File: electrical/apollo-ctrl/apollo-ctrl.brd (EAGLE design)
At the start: 100 x 80 mm, 24 parts, among them J1 BARREL-JACK, Q1 N-chan, U1 NANO

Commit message: DIY version of PCB sort of done, require review
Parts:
- added BAT1: (no value), apollo-ctrl:BATTERY-AA-KIT
- added C1: 47u or more, apollo-ctrl:CPOL-RADIAL-1000UF-25V
- added C2: 100n, apollo-ctrl:CAP-PTH-SMALL
- added COIL2: (no value), apollo-ctrl:SCREWTERMINAL-3.5MM-2
- added D10, D11, D12: 3V6, apollo-ctrl:DIODE-1N4148
- added D4, D5: (no value), apollo-ctrl:DIODE-1N4001
- added D6, D7, D8, D9: (no value), apollo-ctrl:DIODE-1N4148
- added F3: PTC, apollo-ctrl:PTC
- added JP7, JP8: STAND-OFF, apollo-ctrl:STAND-OFF
- added LOGO1: APOLLO-LOGO, apollo-ctrl:APOLLO-LOGO
- added OK2: PC817, apollo-ctrl:DIL04
- added Q2: N-chan, apollo-ctrl:TO220V
- added R10, R11, R12, R13, R14, R15, R7, R8: 620R, apollo-ctrl:AXIAL-0.4
- added R6, R9: 10K, apollo-ctrl:AXIAL-0.4
- added S1: (no value), apollo-ctrl:TACTILE-PTH
- added TVS3, TVS4, TVS5, TVS6, TVS7: TVS 16V, apollo-ctrl:DIODE-1N4148
- added U2: HONEYWELL-MPR, apollo-ctrl:HONEYWELL-MPR-GAGE-DIY
- added X2: SENSOR-O2, apollo-ctrl:JST-PH-4-VERT
- added X3: (no value), apollo-ctrl:1X05
- D1: value (none) -> 3V6
- D2: device apollo-ctrl:DIODE-1N4148 -> apollo-ctrl:DIODE-1N4001
- F1: value PTC -> FUSE 3A; device apollo-ctrl:PTC -> apollo-ctrl:FUSE-KEYSTONE-3568
- F2: value FUSE 3A -> PTC; device apollo-ctrl:FUSE-KEYSTONE-3568 -> apollo-ctrl:PTC
- LED1: value (none) -> GRN
- LED2: value (none) -> RED
- R1: value 1K -> 470R 500mW; device apollo-ctrl:AXIAL-0.4 -> apollo-ctrl:AXIAL-0.5
- R5: value 1K -> 4K7
- SG1: value BUZZER-POL-AI-3035 -> BUZZER
- TVS1: device apollo-ctrl:SMA-DIODE -> apollo-ctrl:DIODE-1N4148
- TVS2: value TVS -> TVS 16V; device apollo-ctrl:SMA-DIODE -> apollo-ctrl:DIODE-1N4148
- moved D2 125.7 mm to (50.0, 52.5)
- moved R5 108.9 mm to (19.5, 49.5)
- moved R4 106.4 mm to (19.5, 52.0)
- moved TVS2 94.0 mm to (69.5, 14.0), turned to 180 degrees
- moved JP3 94.0 mm to (97.0, 77.0)
- moved JP4 94.0 mm to (3.00, 77.0)
- moved TVS1 90.3 mm to (69.5, 11.5)
- moved OK1 90.0 mm to (69.5, 26.5)
- moved D1 84.9 mm to (50.0, 50.0), turned to 180 degrees
- moved LED1 77.2 mm to (58.0, 77.0), turned to 180 degrees
- moved LED2 77.2 mm to (65.0, 77.0), turned to 180 degrees
- moved COIL1 71.6 mm to (67.5, 4.00)
- moved R1 65.2 mm to (50.0, 45.0), turned to 180 degrees
- moved Q1 63.1 mm to (61.0, 15.0), turned to 270 degrees
- moved F1 63.1 mm to (22.0, 11.0)
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- renumbered J1 to X1
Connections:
- removed net N$1: COIL1.2, D1.C, TVS2.C
- new net 3.3V: C2.1, R4.P$2, R5.P$2, U1.3.3V, U2.12
- new net 5V: D4.C, U1.5V, X2.4, X3.5
- new net AUX: U1.D12, X3.2
- new net BUTTON: S1.1, S1.2, TVS5.C, U1.D11
- new net BUZZ: SG1.P, U1.D8
- new net COIL-2: R10.P$1, R9.P$2, U1.D6
- new net COIL-2-CHECK: OK2.4, U1.D7
- new net LED-G: R12.P$2, U1.D10
- new net LED-R: R13.P$2, U1.D9
- new net MCU-TO-O2: R14.P$2, U1.D3
- new net N$10: COIL2.1, D8.A, D9.A, F3.2, TVS4.C
- new net N$11: F3.1, Q2.2
- new net N$12: D9.C, R11.P$1
- new net N$13: D3.C, D5.A, F1.2A, F1.2B, R2.P$2
- new net N$14: BAT1.PWR@1, D2.C, D4.A
- new net N$15: LED2.A, R13.P$1
- new net N$16: LED1.A, R12.P$1
- new net N$17: R14.P$1, TVS6.C, X2.3
- new net N$18: R15.P$1, TVS7.C, X2.2
- new net N$19: D1.C, D2.A, R1.P$1
- new net N$8: OK2.1, R11.P$2
- new net N$9: Q2.1, R10.P$2
- new net O2-TO-MCU: R15.P$2, U1.D2
- new net SCL: D10.C, R4.P$1, U1.A5, U2.3, X3.4
- new net SDA: D11.C, R5.P$1, U1.A4, U2.2, X3.3
- net +12V: now also C1.1, COIL1.2, COIL2.2, D5.C, D6.C, D8.C, R1.P$2, TVS1.C, TVS3.C, U1.RAW; no longer D3.C, F2.2A, F2.2B, R4.P$2
- net COIL-1: now also R6.P$2, R7.P$1, U1.D4; no longer R1.P$1, R2.P$2
- net COIL-1-CHECK: now also U1.D5
- net GND: now also BAT1.GND@1, C1.2, C2.2, D1.A, D10.A, D11.A, D12.A, LED1.K, LED2.K, OK2.2, OK2.3, Q2.3, R3.P$1, R6.P$1, R9.P$1, S1.3, S1.4, SG1.N, TVS3.A, TVS4.A, TVS5.A, TVS6.A, TVS7.A, U1.GND, U1.GND1, U2.10, X2.1, X3.1; no longer R2.P$1, R5.P$1
- net N$2: now also F2.1; no longer F1.P$1
- net N$3: now also R7.P$2; no longer R1.P$2
- net N$4: now also R8.P$2; no longer R3.P$2
- net N$5: now also D6.A, D7.A, F2.2, TVS2.C; no longer D1.A, D2.A, F1.P$2, TVS1.C
- net N$6: now also F1.1A, F1.1B; no longer F2.1A, F2.1B
- net N$7: now also D7.C, R8.P$1; no longer D2.C, R3.P$1
- net V-MON: now also D12.C, R2.P$1, R3.P$2, U1.A3; no longer R4.P$1, R5.P$2
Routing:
- net +12V: track 0.00 -> 110.1 mm
- net 5V: track 0.00 -> 103.6 mm, vias 0 -> 1
- net BUZZ: track 0.00 -> 88.5 mm
- net COIL-2-CHECK: track 0.00 -> 83.9 mm
- net BUTTON: track 0.00 -> 81.1 mm, vias 0 -> 1
- net SCL: track 0.00 -> 77.1 mm
- net LED-R: track 0.00 -> 76.8 mm
- net SDA: track 0.00 -> 75.6 mm, vias 0 -> 1
- net LED-G: track 0.00 -> 74.6 mm
- net COIL-2: track 0.00 -> 74.1 mm
- net COIL-1-CHECK: track 0.00 -> 57.3 mm
- net AUX: track 0.00 -> 57.1 mm
- net 3.3V: track 0.00 -> 53.0 mm
- net COIL-1: track 0.00 -> 47.5 mm
- net MCU-TO-O2: track 0.00 -> 46.6 mm
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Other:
- board text added: "14400 CELL NOT AA"
- board text added: "5V"
- board text added: "AUX"
- board text added: "GND"
- board text added: "POS+"
- board text added: "SCL"
- board text added: "SDA"

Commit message: added more spare pins to i2c header
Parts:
- C1: value 47u or more -> > 47u
- X3: device apollo-ctrl:1X05 -> apollo-ctrl:1X08
- moved TVS5 21.5 mm to (59.3, 67.0), turned to 90 degrees
- moved R12 1.50 mm to (62.0, 67.0)
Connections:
- removed net AUX: U1.D12, X3.2
- new net AUX1: U1.D12, X3.4
- new net AUX2: U1.A1, X3.5
- new net AUX3: U1.A2, X3.6
- net 5V: now also X3.7; no longer X3.5
- net GND: now also X3.8
- net SCL: now also X3.3; no longer X3.4
- net SDA: now also X3.2; no longer X3.3
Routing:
- net AUX3: track 0.00 -> 71.6 mm, vias 0 -> 1
- net AUX2: track 0.00 -> 70.8 mm, vias 0 -> 1
- net AUX1: track 0.00 -> 64.2 mm, vias 0 -> 2
- net AUX: track 57.1 -> 0.00 mm
- net BUTTON: track 81.1 -> 85.6 mm
- net LED-G: track 74.6 -> 76.1 mm
- net SDA: track 75.6 -> 74.5 mm
- net SCL: track 77.1 -> 76.0 mm
- net N$16: track 5.43 -> 6.05 mm
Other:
- board text added: "+5V"
- board text added: "A6"
- board text added: "A7"
- board text added: "D12"
- board text removed: "5V"
- board text removed: "AUX"

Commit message: fixed wrong battery type
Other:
- board text added: "14500 CELL NOT AA"
- board text removed: "14400 CELL NOT AA"
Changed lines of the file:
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@@
 <layer number="21" name="tPlace" color="7" fill="1" visible="yes" active="yes"/>
 <layer number="22" name="bPlace" color="7" fill="1" visible="yes" active="yes"/>
-<layer number="23" name="tOrigins" color="15" fill="1" visible="yes" active="yes"/>
-<layer number="24" name="bOrigins" color="15" fill="1" visible="yes" active="yes"/>
+<layer number="23" name="tOrigins" color="15" fill="1" visible="no" active="yes"/>
+<layer number="24" name="bOrigins" color="15" fill="1" visible="no" active="yes"/>
 <layer number="25" name="tNames" color="7" fill="1" visible="yes" active="yes"/>
 <layer number="26" name="bNames" color="7" fill="1" visible="yes" active="yes"/>
@@
 <wire x1="100" y1="80" x2="0" y2="80" width="0" layer="20"/>
 <wire x1="0" y1="80" x2="0" y2="0" width="0" layer="20"/>
-<text x="17" y="70" size="1.4224" layer="1" font="vector" ratio="12" align="center-left">14400 CELL
+<text x="17" y="70" size="1.4224" layer="1" font="vector" ratio="12" align="center-left">14500 CELL
 NOT AA</text>
-<text x="17" y="70" size="1.4224" layer="29" font="vector" ratio="12" align="center-left">14400 CELL
+<text x="17" y="70" size="1.4224" layer="29" font="vector" ratio="12" align="center-left">14500 CELL
 NOT AA</text>
 <wire x1="49.7" y1="2" x2="50.3" y2="2" width="0.2032" layer="21"/>
@@
 <via x="30" y="45" extent="1-16" drill="0.3" shape="octagon"/>
 <via x="33" y="45" extent="1-16" drill="0.3" shape="octagon"/>
+<via x="13.4" y="43" extent="1-16" drill="0.3" shape="octagon"/>
+<via x="9.4" y="39" extent="1-16" drill="0.3" shape="octagon"/>
 </signal>
 <signal name="COIL-1-CHECK">

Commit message: changed to use Adafruit MPRLS
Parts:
- removed C2: 100n, apollo-ctrl:CAP-PTH-SMALL
- removed JP7, JP8: STAND-OFF, apollo-ctrl:STAND-OFF
- added SJ1: (no value), apollo-ctrl:SJ_2S-NO
- U2: value HONEYWELL-MPR -> ADAFRUIT-MPRLS; device apollo-ctrl:HONEYWELL-MPR-GAGE-DIY -> apollo-ctrl:ADAFRUIT-MPRLS
- moved D10 12.7 mm to (29.0, 46.1)
- moved D11 11.6 mm to (29.0, 53.6)
- moved U2 10.7 mm to (10.0, 56.5), turned to 180 degrees
- moved R4 10.1 mm to (29.0, 48.6)
- moved R5 9.63 mm to (29.0, 51.1)
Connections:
- new net N$1: SJ1.2, U2.RST
- net 3.3V: no longer C2.1, U2.12
- net 5V: now also U2.VIN
- net AUX1: now also SJ1.1
- net GND: now also U2.GND; no longer C2.2, U2.10
- net SCL: now also U2.SCL; no longer U2.3
- net SDA: now also U2.SDA; no longer U2.2
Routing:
- net 5V: track 103.2 -> 136.7 mm
- net 3.3V: track 53.0 -> 65.5 mm, vias 0 -> 1
- net BUZZ: track 88.5 -> 98.1 mm
- net LED-R: track 76.8 -> 86.5 mm
- net LED-G: track 76.1 -> 84.7 mm
- net BUTTON: track 85.6 -> 93.2 mm
- net AUX1: track 64.2 -> 71.8 mm, vias 2 -> 3
- net SCL: track 76.0 -> 82.1 mm
- net N$1: track 0.00 -> 3.59 mm
- net SDA: track 74.5 -> 75.4 mm, vias 1 -> 0
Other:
- board text added: "VIN"

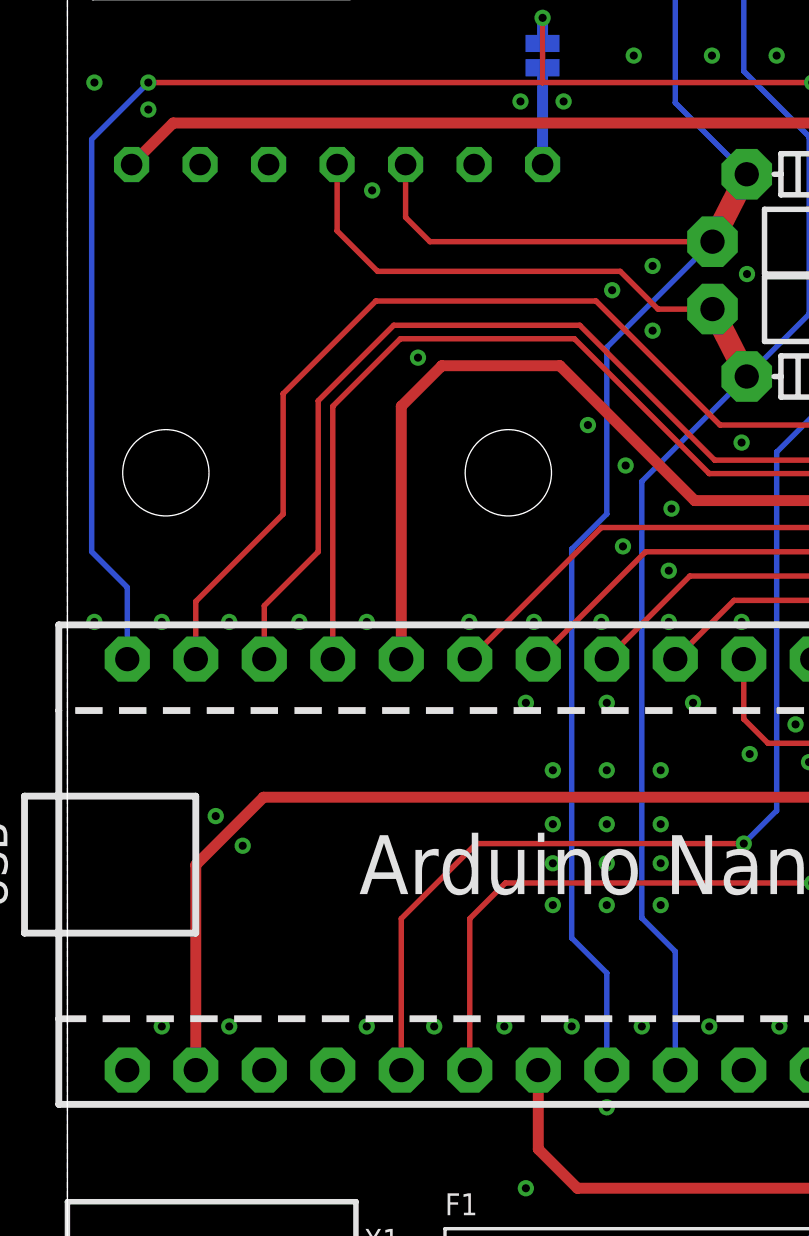
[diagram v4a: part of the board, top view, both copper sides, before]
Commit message: added EOC signal to A0
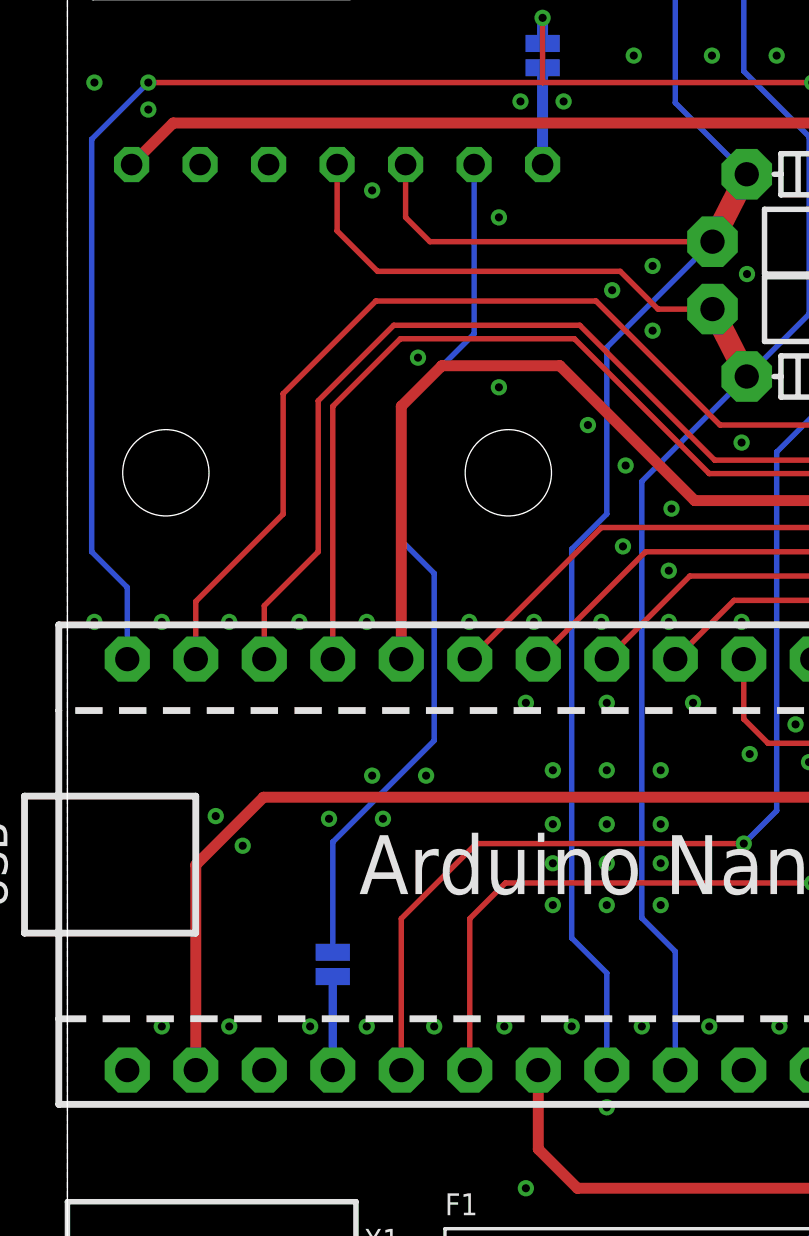
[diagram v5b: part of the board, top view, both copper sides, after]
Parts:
- added SJ2: (no value), apollo-ctrl:SJ_2S-NO
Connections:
- new net A0: SJ2.1, U1.A0
- new net N$20: SJ2.2, U2.EOC
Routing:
- net N$20: track 0.00 -> 32.4 mm
- net A0: track 0.00 -> 3.47 mm
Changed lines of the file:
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@@
 <attribute name="VALUE" x="19.271" y="58.908" size="0.4064" layer="28" rot="MR270"/>
+</element>
+<element name="SJ2" library="apollo-ctrl" package="SJ_2S-NO" value="" x="9.84" y="24.3" smashed="yes" rot="MR90">
+<attribute name="NAME" x="11.11" y="24.392" size="0.8128" layer="26" rot="MR90" align="bottom-center"/>
+<attribute name="VALUE" x="8.189" y="23.392" size="0.4064" layer="28" rot="MR90"/>
 </element>
 </elements>
@@
 <via x="16.8" y="56.3" extent="1-16" drill="0.3" shape="octagon"/>
 <via x="18.4" y="56.3" extent="1-16" drill="0.3" shape="octagon"/>
+<via x="9" y="22" extent="1-16" drill="0.3" shape="octagon"/>
+<via x="9.7" y="29.7" extent="1-16" drill="0.3" shape="octagon"/>
+<via x="11.7" y="29.7" extent="1-16" drill="0.3" shape="octagon"/>
+<via x="13.3" y="31.3" extent="1-16" drill="0.3" shape="octagon"/>
+<via x="11.3" y="31.3" extent="1-16" drill="0.3" shape="octagon"/>
+<via x="16" y="45.7" extent="1-16" drill="0.3" shape="octagon"/>
+<via x="16" y="52" extent="1-16" drill="0.3" shape="octagon"/>
 </signal>
 <signal name="COIL-1-CHECK">
@@
 <wire x1="17.62" y1="53.96" x2="17.62" y2="57.55" width="0.4064" layer="16"/>
 </signal>
+<signal name="A0">
+<contactref element="U1" pad="A0"/>
+<contactref element="SJ2" pad="1"/>
+<wire x1="9.84" y1="20.38" x2="9.84" y2="23.85" width="0.3048" layer="16"/>
+</signal>
+<signal name="N$20">
+<contactref element="U2" pad="EOC"/>
+<contactref element="SJ2" pad="2"/>
+<wire x1="9.84" y1="24.75" x2="9.84" y2="28.84" width="0.2032" layer="16"/>
+<wire x1="9.84" y1="28.84" x2="13.6" y2="32.6" width="0.2032" layer="16"/>
+<wire x1="13.6" y1="32.6" x2="13.6" y2="38.8" width="0.2032" layer="16"/>
+<wire x1="13.6" y1="38.8" x2="12.4" y2="40" width="0.2032" layer="16"/>
+<wire x1="12.4" y1="40" x2="12.4" y2="45" width="0.2032" layer="16"/>
+<wire x1="12.4" y1="45" x2="15.08" y2="47.68" width="0.2032" layer="16"/>
+<wire x1="15.08" y1="47.68" x2="15.08" y2="53.96" width="0.2032" layer="16"/>
+</signal>
 </signals>

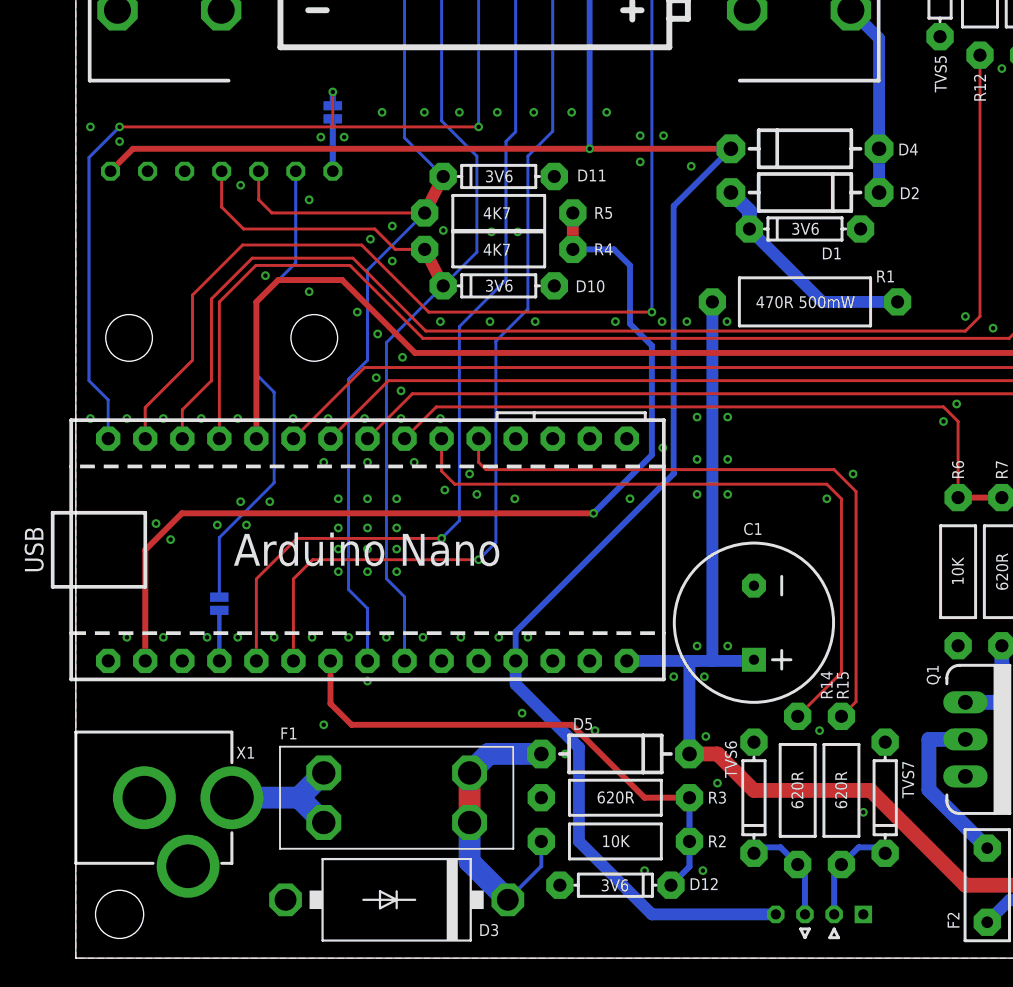
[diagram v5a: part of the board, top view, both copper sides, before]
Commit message: all components now top side
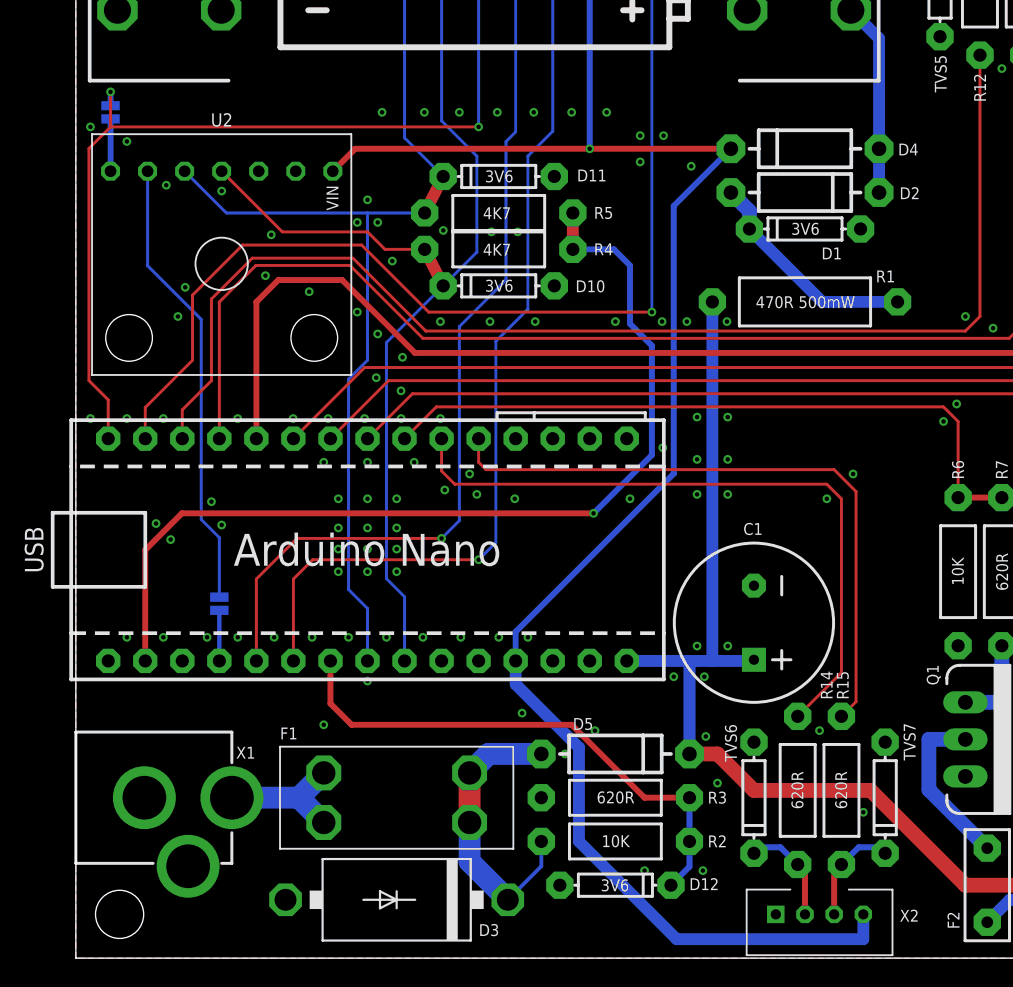
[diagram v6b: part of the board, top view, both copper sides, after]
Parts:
- moved SJ1 15.2 mm to (2.38, 58.0)
- flipped U2 to the top
- flipped X2 to the top
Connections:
- net MCU-TO-O2: now also R15.P$2, U1.D2; no longer R14.P$2, U1.D3
- net N$17: now also X2.2; no longer X2.3
- net N$18: now also X2.3; no longer X2.2
- net O2-TO-MCU: now also R14.P$2, U1.D3; no longer R15.P$2, U1.D2
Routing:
- net 5V: track 136.7 -> 129.8 mm
- net O2-TO-MCU: track 44.2 -> 46.6 mm
- net MCU-TO-O2: track 46.6 -> 44.2 mm
- net SDA: track 75.4 -> 77.7 mm
- net SCL: track 82.1 -> 80.6 mm
- net N$20: track 32.4 -> 31.2 mm
- net AUX1: track 71.8 -> 72.1 mm, vias 3 -> 2
